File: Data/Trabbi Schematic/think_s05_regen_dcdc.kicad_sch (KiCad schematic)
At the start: 4 parts, among them U1 DC/DC Converter (E07), U2 HV Distribution Box

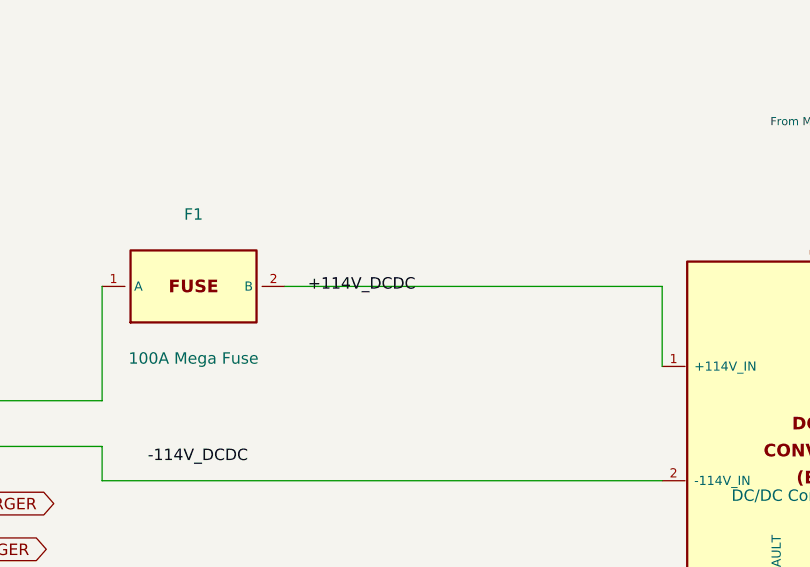
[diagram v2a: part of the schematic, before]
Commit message: Add relay coil/switch graphics, fix label positioning
- Draw coil (inductor arcs) and switch contacts (circles + arm)
  inside RELAY_SPST and RELAY_SPDT symbol bodies
- Add body_gfx parameter to defsym() for custom symbol graphics
- Helper functions: _gfx_polyline, _gfx_arc, _gfx_circle, _relay_gfx
- Fix label offsets: increase from 3-5mm to 10-12mm to avoid
  overlapping pin names (S01 ignition, S02 HV, S05 DCDC, S07 lights)
- Fix S09 turn signal rear labels: add wire stubs (were at 0 offset)
- All 14 schematics regenerated, parentheses balanced, grid OK

Co-Authored-By: Claude Opus 4.6 <noreply@anthropic.com>
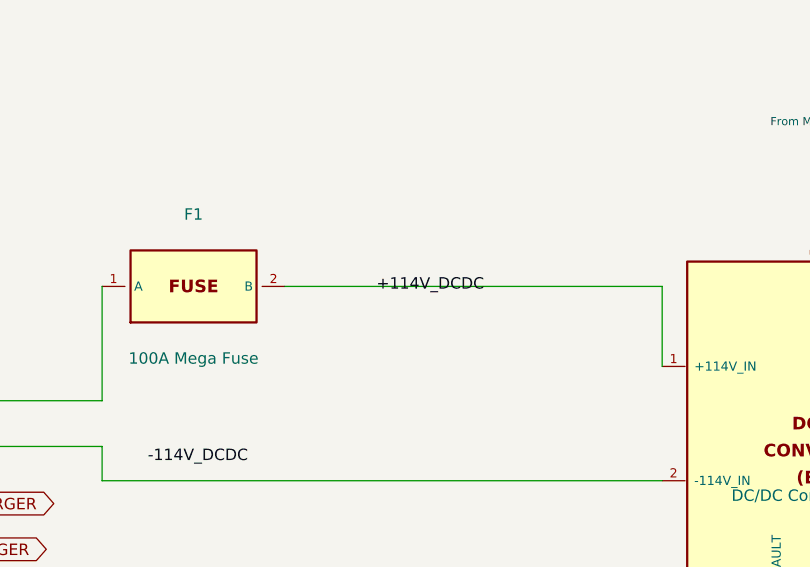
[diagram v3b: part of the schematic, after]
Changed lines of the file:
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@@
     (stroke (width 0) (type default))
   )
-  (label "+114V_DCDC" (at 142.240 85.090 0)
+  (label "+114V_DCDC" (at 149.860 85.090 0)
     (effects (font (size 1.27 1.27)))
   )

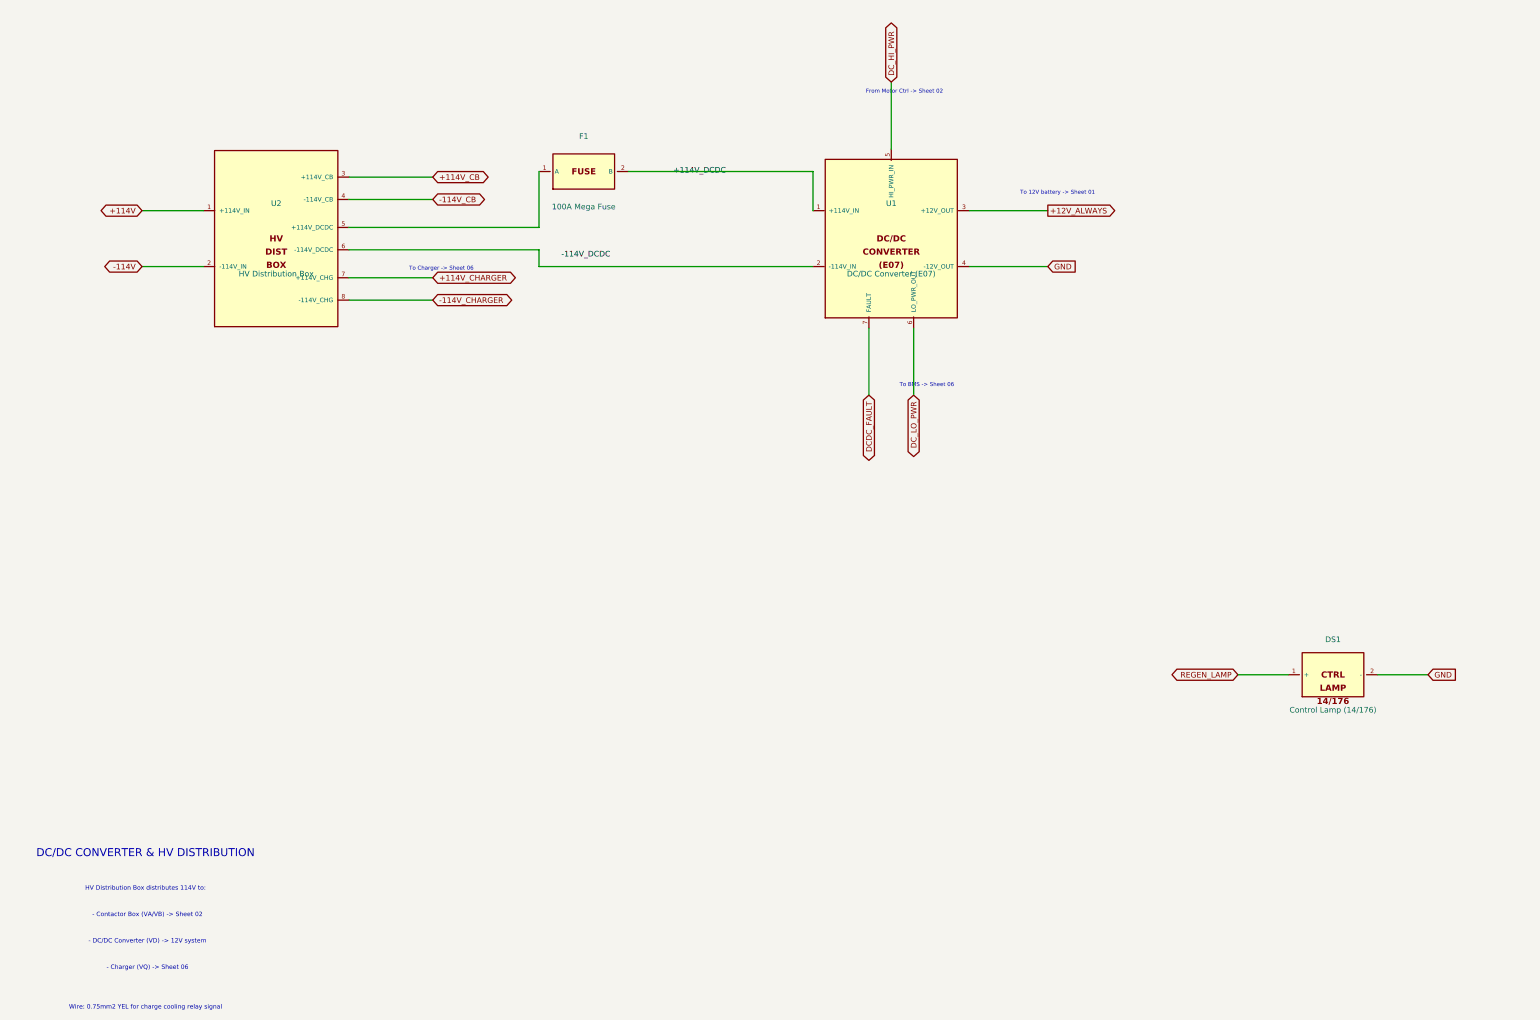
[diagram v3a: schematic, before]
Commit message: Fix label/text positioning: Ref/Value outside body, hide pin numbers
- Reference placed above body edge, Value below (dynamic based on
  symbol height) — no longer overlapping body text
- Pin numbers hidden (clutter, not useful in schematic view)
- Pin name font reduced from 1.016mm to 0.762mm (less overlap)
- Pin length increased from 2.54mm to 3.81mm (more room for pin names
  between body edge and endpoint)
- Store symbol dimensions in _sym_dims for dynamic property placement

Co-Authored-By: Claude Opus 4.6 <noreply@anthropic.com>
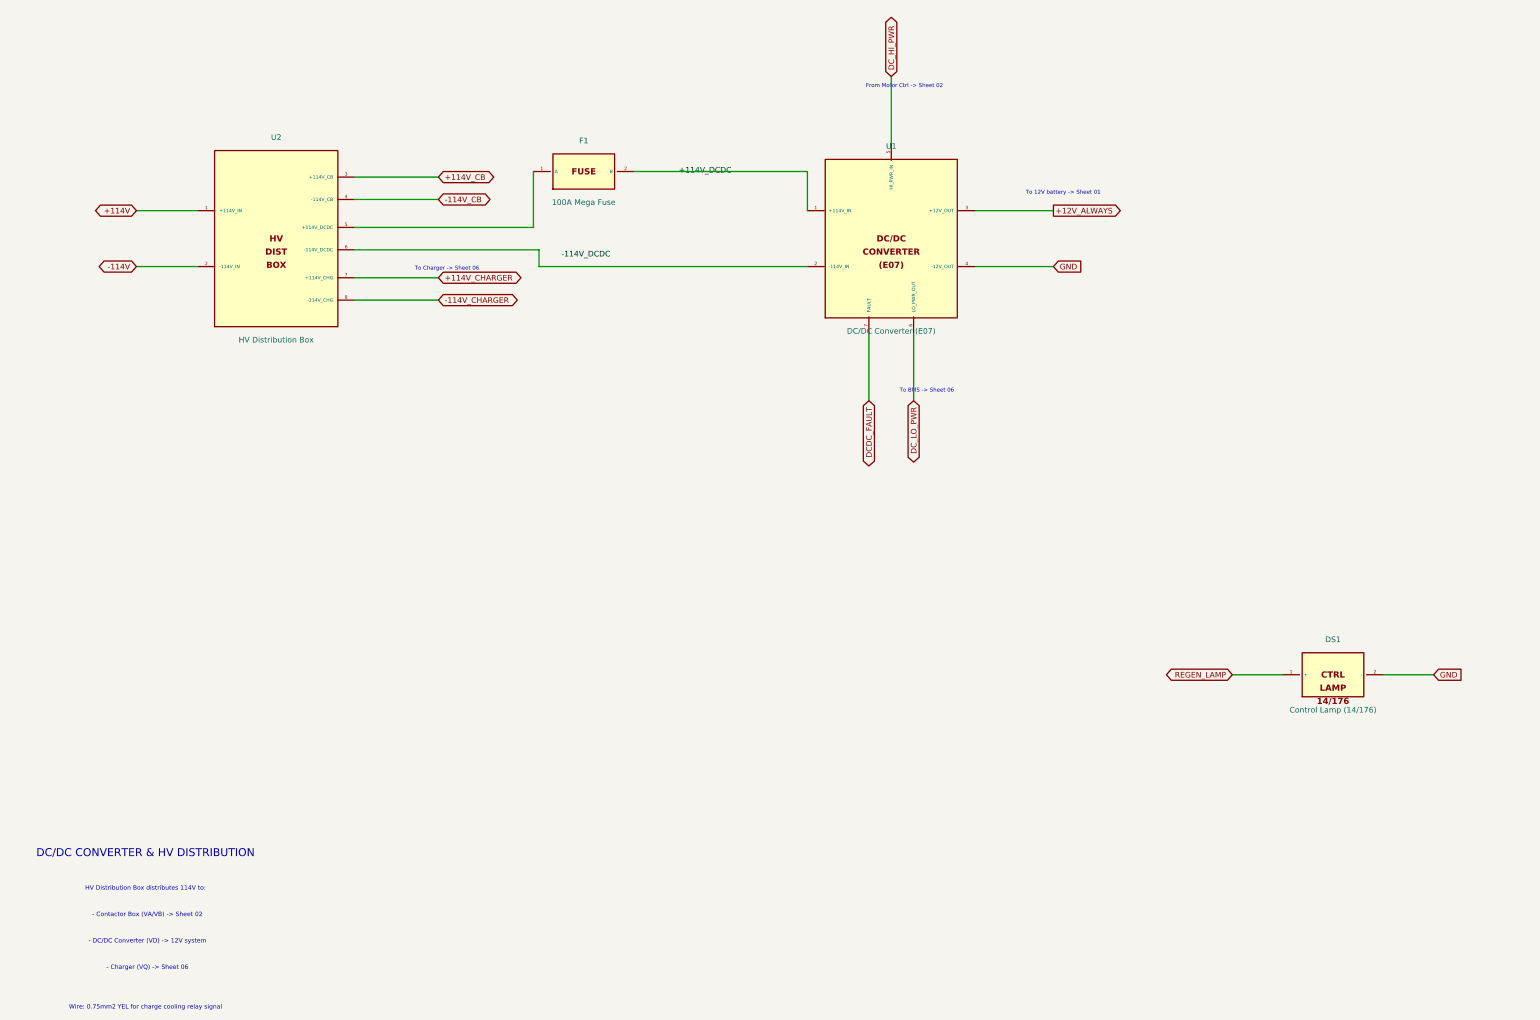
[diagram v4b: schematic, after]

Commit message: Add cross-sheet reference annotations to global labels
- Track all global label positions per sheet during build
- After building all sheets, annotate each global label with
  "→S01,S03,..." text showing which other sheets share the net
- 60 cross-sheet nets identified and annotated
- Two-pass build: 1) build all sheets 2) add cross-refs + save
- Text placed near label in 0.8mm font, offset to avoid overlap

Co-Authored-By: Claude Opus 4.6 <noreply@anthropic.com>
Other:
- note added: "→S01,S02,S03,S04,S06,S07,S08,S09,S10,S11,S12,S13"
- note added: "→S01,S11"
- note added: "→S02,S13"
- note added: "→S04"
- note added: "→S06"
- note added: "→S13"
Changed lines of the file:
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@@
     (effects (font (size 1.000 1.000)))
+  )
+  (text "→S01,S11" (at 239.220 96.480 0)
+    (effects (font (size 0.800 0.800)))
+  )
+  (text "→S01,S02,S03,S04,S06,S07,S08,S09,S10,S11,S12,S13" (at 239.220 109.180 0)
+    (effects (font (size 0.800 0.800)))
+  )
+  (text "→S01,S02,S03,S04,S06,S07,S08,S09,S10,S11,S12,S13" (at 325.580 201.890 0)
+    (effects (font (size 0.800 0.800)))
+  )
+  (text "→S04" (at 202.390 61.500 0)
+    (effects (font (size 0.800 0.800)))
+  )
+  (text "→S06" (at 207.470 139.160 0)
+    (effects (font (size 0.800 0.800)))
+  )
+  (text "→S02,S13" (at 24.940 96.480 0)
+    (effects (font (size 0.800 0.800)))
+  )
+  (text "→S13" (at 24.940 109.180 0)
+    (effects (font (size 0.800 0.800)))
+  )
+  (text "→S06" (at 99.520 111.720 0)
+    (effects (font (size 0.800 0.800)))
+  )
+  (text "→S06" (at 99.520 116.800 0)
+    (effects (font (size 0.800 0.800)))
   )
   (symbol_instances)

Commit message: Fix label text justification for KiCad 9
Add (justify left) to all label and global_label effects.
KiCad 9 requires explicit text justification — without it,
label text is mispositioned relative to the label shape.

Co-Authored-By: Claude Opus 4.6 <noreply@anthropic.com>
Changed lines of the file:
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@@
   )
   (label "+114V_DCDC" (at 151.130 85.090 0)
-    (effects (font (size 1.27 1.27)))
+    (effects (font (size 1.27 1.27)) (justify left))
   )
   (wire (pts (xy 77.470 102.870) (xy 119.380 102.870))
@@
   )
   (label "-114V_DCDC" (at 124.460 104.140 0)
-    (effects (font (size 1.27 1.27)))
+    (effects (font (size 1.27 1.27)) (justify left))
   )
   (wire (pts (xy 218.440 93.980) (xy 236.220 93.980))
@@
   )
   (global_label "+12V_ALWAYS" (shape output) (at 236.220 93.980 0)
-    (effects (font (size 1.27 1.27)))
+    (effects (font (size 1.27 1.27)) (justify left))
     (property "Intersheetrefs" "${INTERSHEET_REFS}" (at 236.220 93.980 0)
       (effects (font (size 1.27 1.27)) hide)
@@
   )
   (global_label "GND" (shape input) (at 236.220 106.680 0)
-    (effects (font (size 1.27 1.27)))
+    (effects (font (size 1.27 1.27)) (justify left))
     (property "Intersheetrefs" "${INTERSHEET_REFS}" (at 236.220 106.680 0)
       (effects (font (size 1.27 1.27)) hide)
@@
   )
   (global_label "DC_HI_PWR" (shape bidirectional) (at 199.390 63.500 90)
-    (effects (font (size 1.27 1.27)))
+    (effects (font (size 1.27 1.27)) (justify left))
     (property "Intersheetrefs" "${INTERSHEET_REFS}" (at 199.390 63.500 0)
       (effects (font (size 1.27 1.27)) hide)
@@
   )
   (global_label "DC_LO_PWR" (shape bidirectional) (at 204.470 137.160 270)
-    (effects (font (size 1.27 1.27)))
+    (effects (font (size 1.27 1.27)) (justify left))
     (property "Intersheetrefs" "${INTERSHEET_REFS}" (at 204.470 137.160 0)
       (effects (font (size 1.27 1.27)) hide)
@@
   )
   (global_label "DCDC_FAULT" (shape bidirectional) (at 194.310 137.160 270)
-    (effects (font (size 1.27 1.27)))
+    (effects (font (size 1.27 1.27)) (justify left))
     (property "Intersheetrefs" "${INTERSHEET_REFS}" (at 194.310 137.160 0)
       (effects (font (size 1.27 1.27)) hide)
@@
   )
   (global_label "+114V" (shape bidirectional) (at 27.940 93.980 180)
-    (effects (font (size 1.27 1.27)))
+    (effects (font (size 1.27 1.27)) (justify left))
     (property "Intersheetrefs" "${INTERSHEET_REFS}" (at 27.940 93.980 0)
       (effects (font (size 1.27 1.27)) hide)
@@
   )
   (global_label "-114V" (shape bidirectional) (at 27.940 106.680 180)
-    (effects (font (size 1.27 1.27)))
+    (effects (font (size 1.27 1.27)) (justify left))
     (property "Intersheetrefs" "${INTERSHEET_REFS}" (at 27.940 106.680 0)
       (effects (font (size 1.27 1.27)) hide)
@@
   )
   (global_label "+114V_CB" (shape bidirectional) (at 96.520 86.360 0)
-    (effects (font (size 1.27 1.27)))
+    (effects (font (size 1.27 1.27)) (justify left))
     (property "Intersheetrefs" "${INTERSHEET_REFS}" (at 96.520 86.360 0)
       (effects (font (size 1.27 1.27)) hide)
@@
   )
   (global_label "-114V_CB" (shape bidirectional) (at 96.520 91.440 0)
-    (effects (font (size 1.27 1.27)))
+    (effects (font (size 1.27 1.27)) (justify left))
     (property "Intersheetrefs" "${INTERSHEET_REFS}" (at 96.520 91.440 0)
       (effects (font (size 1.27 1.27)) hide)
@@
   )
   (global_label "+114V_CHARGER" (shape bidirectional) (at 96.520 109.220 0)
-    (effects (font (size 1.27 1.27)))
+    (effects (font (size 1.27 1.27)) (justify left))
     (property "Intersheetrefs" "${INTERSHEET_REFS}" (at 96.520 109.220 0)
       (effects (font (size 1.27 1.27)) hide)
@@
   )
   (global_label "-114V_CHARGER" (shape bidirectional) (at 96.520 114.300 0)
-    (effects (font (size 1.27 1.27)))
+    (effects (font (size 1.27 1.27)) (justify left))
     (property "Intersheetrefs" "${INTERSHEET_REFS}" (at 96.520 114.300 0)
       (effects (font (size 1.27 1.27)) hide)
@@
   )
   (global_label "REGEN_LAMP" (shape bidirectional) (at 276.860 199.390 180)
-    (effects (font (size 1.27 1.27)))
+    (effects (font (size 1.27 1.27)) (justify left))
     (property "Intersheetrefs" "${INTERSHEET_REFS}" (at 276.860 199.390 0)
       (effects (font (size 1.27 1.27)) hide)
@@
   )
   (global_label "GND" (shape input) (at 322.580 199.390 0)
-    (effects (font (size 1.27 1.27)))
+    (effects (font (size 1.27 1.27)) (justify left))
     (property "Intersheetrefs" "${INTERSHEET_REFS}" (at 322.580 199.390 0)
       (effects (font (size 1.27 1.27)) hide)

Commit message: Relay symbol for flasher, label justify set to auto
- Flasher Relay (Think:FLASHER_RELAY) now has coil+switch graphics
  matching the standard relay symbol style
- All relays (SPST, SPDT, Flasher) use consistent coil+switch body
- Remove (justify left) from all label and global_label effects —
  KiCad 9 auto-determines text alignment based on label orientation

Co-Authored-By: Claude Opus 4.6 <noreply@anthropic.com>
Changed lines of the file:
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@@
   )
   (label "+114V_DCDC" (at 151.130 85.090 0)
-    (effects (font (size 1.27 1.27)) (justify left))
+    (effects (font (size 1.27 1.27)))
   )
   (wire (pts (xy 77.470 102.870) (xy 119.380 102.870))
@@
   )
   (label "-114V_DCDC" (at 124.460 104.140 0)
-    (effects (font (size 1.27 1.27)) (justify left))
+    (effects (font (size 1.27 1.27)))
   )
   (wire (pts (xy 218.440 93.980) (xy 236.220 93.980))
@@
   )
   (global_label "+12V_ALWAYS" (shape output) (at 236.220 93.980 0)
-    (effects (font (size 1.27 1.27)) (justify left))
+    (effects (font (size 1.27 1.27)))
     (property "Intersheetrefs" "${INTERSHEET_REFS}" (at 236.220 93.980 0)
       (effects (font (size 1.27 1.27)) hide)
@@
   )
   (global_label "GND" (shape input) (at 236.220 106.680 0)
-    (effects (font (size 1.27 1.27)) (justify left))
+    (effects (font (size 1.27 1.27)))
     (property "Intersheetrefs" "${INTERSHEET_REFS}" (at 236.220 106.680 0)
       (effects (font (size 1.27 1.27)) hide)
@@
   )
   (global_label "DC_HI_PWR" (shape bidirectional) (at 199.390 63.500 90)
-    (effects (font (size 1.27 1.27)) (justify left))
+    (effects (font (size 1.27 1.27)))
     (property "Intersheetrefs" "${INTERSHEET_REFS}" (at 199.390 63.500 0)
       (effects (font (size 1.27 1.27)) hide)
@@
   )
   (global_label "DC_LO_PWR" (shape bidirectional) (at 204.470 137.160 270)
-    (effects (font (size 1.27 1.27)) (justify left))
+    (effects (font (size 1.27 1.27)))
     (property "Intersheetrefs" "${INTERSHEET_REFS}" (at 204.470 137.160 0)
       (effects (font (size 1.27 1.27)) hide)
@@
   )
   (global_label "DCDC_FAULT" (shape bidirectional) (at 194.310 137.160 270)
-    (effects (font (size 1.27 1.27)) (justify left))
+    (effects (font (size 1.27 1.27)))
     (property "Intersheetrefs" "${INTERSHEET_REFS}" (at 194.310 137.160 0)
       (effects (font (size 1.27 1.27)) hide)
@@
   )
   (global_label "+114V" (shape bidirectional) (at 27.940 93.980 180)
-    (effects (font (size 1.27 1.27)) (justify left))
+    (effects (font (size 1.27 1.27)))
     (property "Intersheetrefs" "${INTERSHEET_REFS}" (at 27.940 93.980 0)
       (effects (font (size 1.27 1.27)) hide)
@@
   )
   (global_label "-114V" (shape bidirectional) (at 27.940 106.680 180)
-    (effects (font (size 1.27 1.27)) (justify left))
+    (effects (font (size 1.27 1.27)))
     (property "Intersheetrefs" "${INTERSHEET_REFS}" (at 27.940 106.680 0)
       (effects (font (size 1.27 1.27)) hide)
@@
   )
   (global_label "+114V_CB" (shape bidirectional) (at 96.520 86.360 0)
-    (effects (font (size 1.27 1.27)) (justify left))
+    (effects (font (size 1.27 1.27)))
     (property "Intersheetrefs" "${INTERSHEET_REFS}" (at 96.520 86.360 0)
       (effects (font (size 1.27 1.27)) hide)
@@
   )
   (global_label "-114V_CB" (shape bidirectional) (at 96.520 91.440 0)
-    (effects (font (size 1.27 1.27)) (justify left))
+    (effects (font (size 1.27 1.27)))
     (property "Intersheetrefs" "${INTERSHEET_REFS}" (at 96.520 91.440 0)
       (effects (font (size 1.27 1.27)) hide)
@@
   )
   (global_label "+114V_CHARGER" (shape bidirectional) (at 96.520 109.220 0)
-    (effects (font (size 1.27 1.27)) (justify left))
+    (effects (font (size 1.27 1.27)))
     (property "Intersheetrefs" "${INTERSHEET_REFS}" (at 96.520 109.220 0)
       (effects (font (size 1.27 1.27)) hide)
@@
   )
   (global_label "-114V_CHARGER" (shape bidirectional) (at 96.520 114.300 0)
-    (effects (font (size 1.27 1.27)) (justify left))
+    (effects (font (size 1.27 1.27)))
     (property "Intersheetrefs" "${INTERSHEET_REFS}" (at 96.520 114.300 0)
       (effects (font (size 1.27 1.27)) hide)
@@
   )
   (global_label "REGEN_LAMP" (shape bidirectional) (at 276.860 199.390 180)
-    (effects (font (size 1.27 1.27)) (justify left))
+    (effects (font (size 1.27 1.27)))
     (property "Intersheetrefs" "${INTERSHEET_REFS}" (at 276.860 199.390 0)
       (effects (font (size 1.27 1.27)) hide)
@@
   )
   (global_label "GND" (shape input) (at 322.580 199.390 0)
-    (effects (font (size 1.27 1.27)) (justify left))
+    (effects (font (size 1.27 1.27)))
     (property "Intersheetrefs" "${INTERSHEET_REFS}" (at 322.580 199.390 0)
       (effects (font (size 1.27 1.27)) hide)
